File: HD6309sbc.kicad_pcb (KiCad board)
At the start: 4 copper layers, 99.8 x 99.8 mm, 63 parts, among them J1 Conn_01x02_Male, J2 Conn_02x30_Odd_Even, J3 Conn_01x02_Male, J4 Conn_01x07_Socket, J5 Conn_01x07_Socket, SW1 SW_Push, U1 HD63C09, U12 74HCT138, U16 74HCT541, U17 74HCT00, U18 74HCT04, U19 74HCT30, U2 DS1813, U3 74AHC1G14, U7 74HCT574

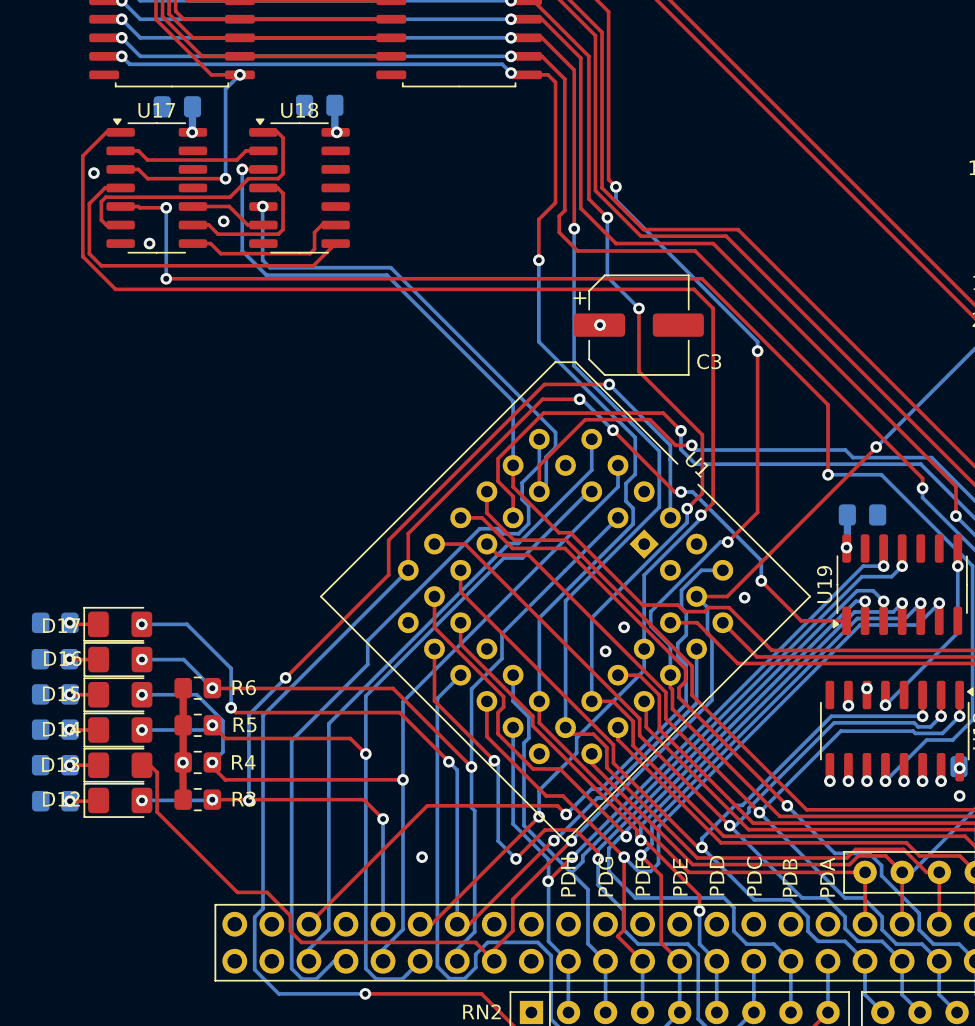
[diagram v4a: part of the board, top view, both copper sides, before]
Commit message: disambiguate register address
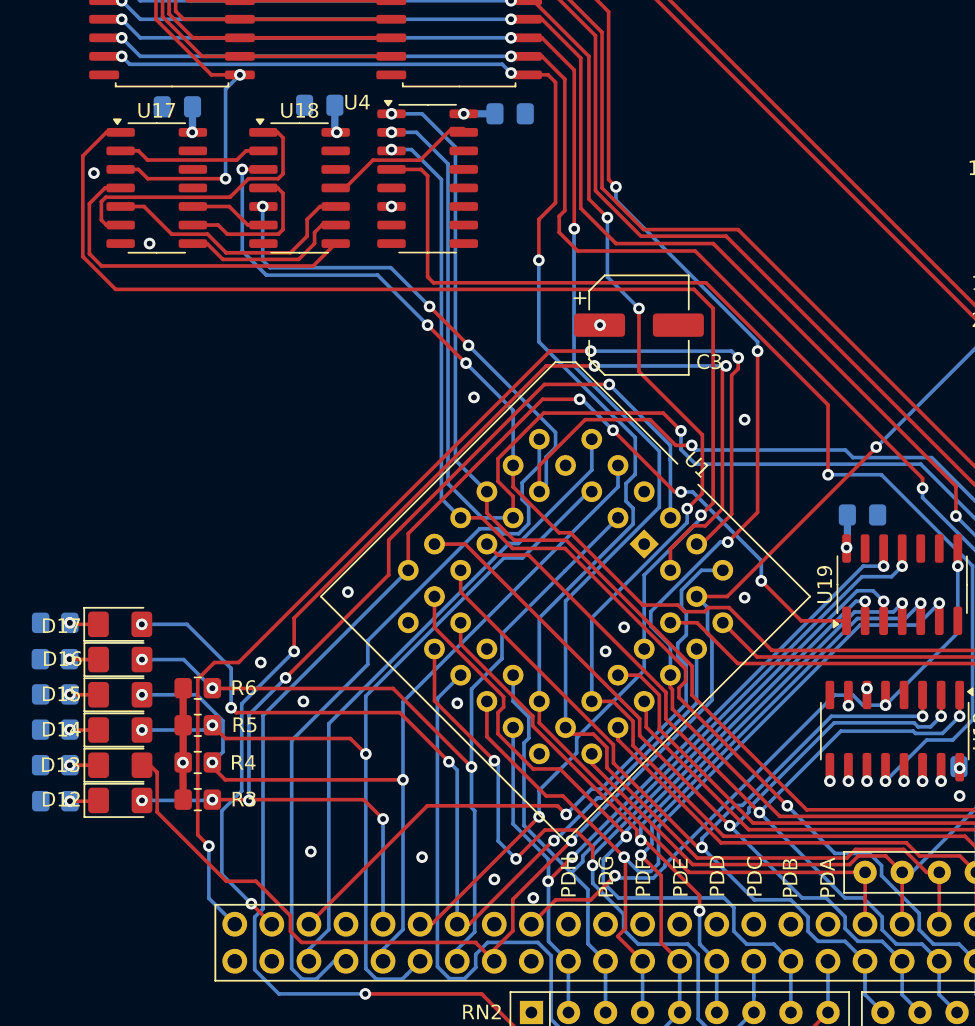
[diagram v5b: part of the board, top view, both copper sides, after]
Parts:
- added C8: 10uF, Capacitor_SMD:C_0805_2012Metric_Pad1.18x1.45mm_HandSolder, B.Cu at (64.1, 62.0)
- added U4: 74HCT138, Package_SO:SOIC-16_3.9x9.9mm_P1.27mm, F.Cu at (58.4, 66.4)
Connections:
- net /GPR1/~{SELPD0} renamed /GPR1/~{SELPD00}
- net SELPA renamed ~{SELPA}
- net SELPB renamed ~{SELPB}
- net SELPC renamed ~{SELPC}
- net SELPE renamed ~{SELPE}
- net SELPF renamed ~{SELPF}
- net SELPG renamed ~{SELPG}
- net SELPH renamed ~{SELPH}
- J2 pad 33: SELPD -> ~{SELPD}
- J2 pad 43: unconnected-(J2-Pin_43-Pad43) -> ~{MappedMem}
- J2 pad 57: unconnected-(J2-Pin_57-Pad57) -> TSC
- J2 pad 59: unconnected-(J2-Pin_59-Pad59) -> LIC
- U12 pad 12: SELPD -> ~{SELPD}
- U12 pad 5: /MemoryDecoder/MappedMem -> ~{MappedMem}
- U17 pad 5: SELPD -> Net-(U17-Pad5)
- U18 pad 10: unconnected-(U18-Pad10) -> Net-(U17-Pad5)
- U18 pad 11: unconnected-(U18-Pad11) -> ~{SELPD0}
- U19 pad 8: /MemoryDecoder/MappedMem -> ~{MappedMem}
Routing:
- net SELPD: track 109.3 -> 0.00 mm, vias 4 -> 0
- net ~{SELPD}: track 0.00 -> 92.8 mm, vias 0 -> 2
- net LIC: track 0.00 -> 78.5 mm, vias 0 -> 3
- net TSC: track 0.00 -> 77.2 mm, vias 0 -> 4
- net ~{MappedMem}: track 0.00 -> 44.7 mm, vias 0 -> 3
- net /A3: track 79.2 -> 111.3 mm, vias 1 -> 2
- net /A2: track 63.8 -> 93.6 mm, vias 1 -> 2
- net /A4: track 54.8 -> 82.8 mm, vias 1 -> 2
- net Net-(U17-Pad5): track 0.00 -> 18.0 mm
- net /MemoryDecoder/MappedMem: track 13.5 -> 0.00 mm, vias 2 -> 0
- net ~{SELPD0}: track 0.00 -> 10.5 mm
- net +5V: track 41.5 -> 43.7 mm, vias 10 -> 12
- net /A9: track 70.5 -> 71.3 mm
- net /A10: track 77.2 -> 77.8 mm
- net /A0: track 103.5 -> 103.1 mm, vias 2 -> 4
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
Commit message: tighten up tracing
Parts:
- moved C5 3.68 mm to (58.6, 47.8)
- moved U16 3.68 mm to (56.9, 53.6)
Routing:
- net /intD1: track 94.9 -> 113.3 mm
- net /intD0: track 100.2 -> 114.9 mm
- net /GPR1/W: track 73.3 -> 76.9 mm
- net /D0: track 132.1 -> 130.2 mm
- net /D2: track 146.5 -> 145.4 mm
- net /D1: track 154.4 -> 153.3 mm

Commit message: clean up before redesign
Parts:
- removed U17: 74HCT00, Package_SO:SOIC-14_3.9x8.7mm_P1.27mm
- removed U18: 74HCT04, Package_SO:SOIC-14_3.9x8.7mm_P1.27mm
- added C10: 10uF, Capacitor_SMD:C_0805_2012Metric_Pad1.18x1.45mm_HandSolder, B.Cu at (90.4, 47.9)
- added C9: 10uF, Capacitor_SMD:C_0805_2012Metric_Pad1.18x1.45mm_HandSolder, B.Cu at (78.3, 47.9)
- added D18: LED_Filled, LED_SMD:LED_1206_3216Metric_Pad1.42x1.75mm_HandSolder, F.Cu at (87.5, 37.6)
- added D19: LED_Filled, LED_SMD:LED_1206_3216Metric_Pad1.42x1.75mm_HandSolder, F.Cu at (85.1, 37.6)
- added D20: LED_Filled, LED_SMD:LED_1206_3216Metric_Pad1.42x1.75mm_HandSolder, F.Cu at (82.8, 37.6)
- added D21: LED_Filled, LED_SMD:LED_1206_3216Metric_Pad1.42x1.75mm_HandSolder, F.Cu at (80.4, 37.6)
- added D22: LED_Filled, LED_SMD:LED_1206_3216Metric_Pad1.42x1.75mm_HandSolder, F.Cu at (78.0, 37.6)
- added D23: LED_Filled, LED_SMD:LED_1206_3216Metric_Pad1.42x1.75mm_HandSolder, F.Cu at (75.6, 37.6)
- added D24: LED_Filled, LED_SMD:LED_1206_3216Metric_Pad1.42x1.75mm_HandSolder, F.Cu at (73.2, 37.6)
- added D25: LED_Filled, LED_SMD:LED_1206_3216Metric_Pad1.42x1.75mm_HandSolder, F.Cu at (70.8, 37.6)
- added J6: PD0, Connector_PinSocket_2.54mm:PinSocket_1x08_P2.54mm_Vertical, F.Cu at (62.0, 42.0)
- added J7: PD1, Connector_PinSocket_2.54mm:PinSocket_1x08_P2.54mm_Vertical, F.Cu at (88.0, 42.0)
- added R22: 470R, Resistor_SMD:R_0805_2012Metric_Pad1.20x1.40mm_HandSolder, B.Cu at (87.6, 33.5)
- added R23: 470R, Resistor_SMD:R_0805_2012Metric_Pad1.20x1.40mm_HandSolder, B.Cu at (85.1, 33.5)
- added R24: 470R, Resistor_SMD:R_0805_2012Metric_Pad1.20x1.40mm_HandSolder, B.Cu at (82.8, 33.5)
- added R25: 470R, Resistor_SMD:R_0805_2012Metric_Pad1.20x1.40mm_HandSolder, B.Cu at (80.4, 33.5)
- added R26: 470R, Resistor_SMD:R_0805_2012Metric_Pad1.20x1.40mm_HandSolder, B.Cu at (78.0, 33.5)
- added R27: 470R, Resistor_SMD:R_0805_2012Metric_Pad1.20x1.40mm_HandSolder, B.Cu at (75.6, 33.5)
- added R28: 470R, Resistor_SMD:R_0805_2012Metric_Pad1.20x1.40mm_HandSolder, B.Cu at (73.2, 33.5)
- added R29: 470R, Resistor_SMD:R_0805_2012Metric_Pad1.20x1.40mm_HandSolder, B.Cu at (70.8, 33.5)
- added U5: GAL16V8, Package_DIP:DIP-20_W7.62mm, F.Cu at (29.9, 71.3)
- added U6: 74HCT574, Package_SO:SOIC-20W_7.5x12.8mm_P1.27mm, F.Cu at (76.7, 53.6)
- added U8: 74HCT541, Package_SO:SOIC-20W_7.5x12.8mm_P1.27mm, F.Cu at (88.7, 53.6)
- moved C2 23.3 mm to (28.9, 68.6)
- moved C1 13.4 mm to (28.9, 66.4)
- moved C4 4.04 mm to (47.0, 47.9)
- moved U7 3.97 mm to (44.9, 53.6)
- moved R20 3.54 mm to (29.3, 99.3)
- moved D12 3.54 mm to (33.8, 109.0)
- moved D13 3.54 mm to (33.8, 106.6)
- moved D14 3.54 mm to (33.8, 104.2)
- moved D15 3.54 mm to (33.8, 101.8)
- moved D16 3.54 mm to (33.8, 99.4)
- moved D17 3.54 mm to (33.8, 97.0)
- moved R16 3.54 mm to (29.4, 109.1)
- moved R17 3.54 mm to (29.4, 106.6)
- moved R18 3.54 mm to (29.4, 104.2)
- moved R19 3.54 mm to (29.4, 101.8)
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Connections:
- net /intD0 renamed /ClockCard/intD00
- net /intD1 renamed /ClockCard/intD01
- net /intD2 renamed /ClockCard/intD02
- net /intD3 renamed /ClockCard/intD03
- net /intD4 renamed /ClockCard/intD04
- net /intD5 renamed /ClockCard/intD05
- net /intD6 renamed /ClockCard/intD06
- net /intD7 renamed /ClockCard/intD07
- U16 pad 1: /GPR1/W -> /GPR1/~{R}0
- U4 pad 10: unconnected-(U4-~{Y5}-Pad10) -> ~{SELPD5}
- U4 pad 11: unconnected-(U4-~{Y4}-Pad11) -> ~{SELPD4}
- U4 pad 12: unconnected-(U4-~{Y3}-Pad12) -> ~{SELPD3}
- U4 pad 13: unconnected-(U4-~{Y2}-Pad13) -> ~{SELPD2}
- U4 pad 14: unconnected-(U4-~{Y1}-Pad14) -> ~{SELPD1}
- U4 pad 7: unconnected-(U4-~{Y7}-Pad7) -> ~{SELPD7}
- U4 pad 9: unconnected-(U4-~{Y6}-Pad9) -> ~{SELPD6}
- U7 pad 11: /GPR1/W -> /GPR1/W0
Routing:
- net /GPR1/W: track 76.9 -> 0.00 mm, vias 2 -> 0
- net /GPR1/~{R}0: track 0.00 -> 71.0 mm
- net /GPR1/~{R}1: track 0.00 -> 65.5 mm, vias 0 -> 2
- net E: track 118.8 -> 176.8 mm, vias 2 -> 4
- net /GPR1/W1: track 0.00 -> 43.1 mm, vias 0 -> 2
- net /D0: track 130.2 -> 161.8 mm, vias 5 -> 7
- net /D3: track 123.7 -> 154.9 mm, vias 5 -> 7
- net /D4: track 140.0 -> 171.3 mm, vias 3 -> 5
- net /D2: track 145.4 -> 176.6 mm, vias 3 -> 5
- net /D1: track 153.3 -> 184.6 mm, vias 3 -> 5
- net /D5: track 118.3 -> 149.4 mm, vias 3 -> 5
- net /D6: track 137.4 -> 168.1 mm, vias 3 -> 5
- net /D7: track 112.3 -> 141.8 mm, vias 3 -> 5
- net /intD17: track 0.00 -> 28.6 mm
- net /intD16: track 0.00 -> 25.9 mm
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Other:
- board text added: "BUSY"
- board text added: "FIRQ"
- board text added: "GPR PD1"
- board text added: "HALT"
- board text added: "IRQ"
- board text added: "NMI"
- board text added: "RES"

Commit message: update readme
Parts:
- removed C1, C10, C2, C4, C5, C6, C7, C8, C9: 10uF, Capacitor_SMD:C_0805_2012Metric_Pad1.18x1.45mm_HandSolder
- removed D1: RED, LED_SMD:LED_0805_2012Metric_Pad1.15x1.40mm_HandSolder
- removed D10, D11, D12, D13, D14, D15, D16, D17, D18, D19, D20, D21, D22, D23, D24, D25, D4, D5, D6, D7, D8, D9: LED_Filled, LED_SMD:LED_1206_3216Metric_Pad1.42x1.75mm_HandSolder
- removed D2: YELLOW, LED_SMD:LED_0805_2012Metric_Pad1.15x1.40mm_HandSolder
- removed D3: GREEN, LED_SMD:LED_0805_2012Metric_Pad1.15x1.40mm_HandSolder
- removed J1, J3: Conn_01x02_Male, Connector_PinHeader_2.54mm:PinHeader_1x02_P2.54mm_Vertical
- removed R1, R10, R11, R12, R13, R14, R15, R16, R17, R18, R19, R20, R21, R22, R23, R24, R25, R26, R27, R28, R29: 470R, Resistor_SMD:R_0805_2012Metric_Pad1.20x1.40mm_HandSolder
- removed R2, R9: 330R, Resistor_SMD:R_0805_2012Metric_Pad1.20x1.40mm_HandSolder
- removed RN1, RN2, RN3: 4K7, Resistor_THT:R_Array_SIP9
- removed SW1: SW_Push, Button_Switch_SMD:SW_SPST_B3S-1000
- removed U12, U4: 74HCT138, Package_SO:SOIC-16_3.9x9.9mm_P1.27mm
- removed U16, U8: 74HCT541, Package_SO:SOIC-20W_7.5x12.8mm_P1.27mm
- removed U19: 74HCT30, Package_SO:SOIC-14_3.9x8.7mm_P1.27mm
- removed U2: DS1813, Package_TO_SOT_SMD:SOT-23-3
- removed U3: 74AHC1G14, Package_TO_SOT_SMD:SOT-353_SC-70-5_Handsoldering
- removed U5: GAL16V8, Package_DIP:DIP-20_W7.62mm
- removed U6, U7: 74HCT574, Package_SO:SOIC-20W_7.5x12.8mm_P1.27mm
- added J8: Interrupts, Connector_PinHeader_2.54mm:PinHeader_1x04_P2.54mm_Vertical, B.Cu at (79.6, 33.9)
- J2: value Conn_02x30_Odd_Even -> Address Bus; footprint Connector_PinHeader_2.54mm:PinHeader_2x30_P2.54mm_Vertical -> Connector_PinHeader_2.54mm:PinHeader_1x16_P2.54mm_Vertical; moved to B.Cu
- J4: value Conn_01x07_Socket -> Power; footprint Connector_PinSocket_2.54mm:PinSocket_1x07_P2.54mm_Vertical -> Connector_PinHeader_2.54mm:PinHeader_1x04_P2.54mm_Vertical; moved to B.Cu
- J5: value Conn_01x07_Socket -> quadrature; footprint Connector_PinSocket_2.54mm:PinSocket_1x07_P2.54mm_Vertical -> Connector_PinSocket_2.54mm:PinSocket_1x04_P2.54mm_Vertical; moved to B.Cu
- J6: value PD0 -> Data Bus; footprint Connector_PinSocket_2.54mm:PinSocket_1x08_P2.54mm_Vertical -> Connector_PinHeader_2.54mm:PinHeader_1x08_P2.54mm_Vertical; moved to B.Cu
- J7: value PD1 -> CPU Control; footprint Connector_PinSocket_2.54mm:PinSocket_1x08_P2.54mm_Vertical -> Connector_PinHeader_2.54mm:PinHeader_1x08_P2.54mm_Vertical; moved to B.Cu
- R7: value 470R -> 4.7k; moved to F.Cu
- R8: value 330R -> 4.7k
- moved J2 113.5 mm to (28.6, 48.6), turned to 180 degrees
- moved J4 81.8 mm to (28.6, 42.7), turned to 0 degrees
- moved J5 79.8 mm to (33.8, 86.9), turned to -90 degrees
- moved R5 74.1 mm to (73.9, 36.7)
- moved R4 74.1 mm to (73.9, 39.3)
- moved R3 71.8 mm to (73.9, 44.3)
- moved R6 67.2 mm to (73.9, 41.8)
- moved C3 41.9 mm to (48.2, 42.6), turned to 180 degrees
- moved R8 39.0 mm to (73.9, 46.9), turned to 0 degrees
- moved U1 36.4 mm to (58.2, 58.3)
- moved J6 32.9 mm to (79.4, 69.9), turned to 180 degrees
- moved J7 23.6 mm to (79.4, 63.9), turned to 0 degrees
- moved R7 14.9 mm to (73.9, 33.9), turned to 0 degrees
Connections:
- J2 pad 1: unconnected-(J2-Pin_1-Pad1) -> /A0
- J2 pad 10: Q -> /A9
- J2 pad 11: /D0 -> /A10
- J2 pad 12: /A0 -> /A11
- J2 pad 13: /D1 -> /A12
- J2 pad 14: /A1 -> /A13
- J2 pad 15: /D2 -> /A14
- J2 pad 16: /A2 -> /A15
- J2 pad 2: +5V -> /A1
- J2 pad 3: Clock24 -> /A2
- J2 pad 4: Clock3 -> /A3
- J2 pad 5: Clock12 -> /A4
- J2 pad 6: Clock6 -> /A5
- J2 pad 7: ~{E} -> /A6
- J2 pad 8: E -> /A7
- J2 pad 9: ~{Q} -> /A8
- J4 pad 1: /ClockCard/intD00 -> GND
- J4 pad 2: /ClockCard/intD01 -> +5V
- J4 pad 3: Clock24 -> +5V
- J4 pad 4: Clock12 -> GND
- J5 pad 1: GND -> E
- J5 pad 2: E -> unconnected-(J5-Pin_2-Pad2)
- J5 pad 3: ~{E} -> ~{RESET}
- J5 pad 4: ~{RESET} -> Q
- J6 pad 1: /ClockCard/intD00 -> /D0
- J6 pad 2: /ClockCard/intD01 -> /D1
- J6 pad 3: /ClockCard/intD02 -> /D2
- J6 pad 4: /ClockCard/intD03 -> /D3
- J6 pad 5: /ClockCard/intD04 -> /D4
- J6 pad 6: /ClockCard/intD05 -> /D5
- J6 pad 7: /ClockCard/intD06 -> /D6
- J6 pad 8: /ClockCard/intD07 -> /D7
- J7 pad 1: /intD10 -> BUSY
- J7 pad 2: /intD11 -> R/~{W}
- J7 pad 3: /intD12 -> ~{HALT}
- J7 pad 4: /intD13 -> AVMA
- J7 pad 5: /intD14 -> TSC
- J7 pad 6: /intD15 -> LIC
- J7 pad 7: /intD16 -> BS
- J7 pad 8: /intD17 -> BA
- R7 pad 1: Net-(D5-K) -> +5V
- R7 pad 2: GND -> ~{RESET}
- R8 pad 1: Net-(D2-K) -> TSC
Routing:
- net /D1: track 184.6 -> 25.2 mm, vias 5 -> 0
- net /D2: track 176.6 -> 23.7 mm, vias 5 -> 0
- net /D4: track 171.3 -> 26.8 mm, vias 5 -> 0
- net /D0: track 161.8 -> 20.5 mm, vias 7 -> 0
- net E: track 176.8 -> 36.4 mm, vias 4 -> 0
- net /D6: track 168.1 -> 30.0 mm, vias 5 -> 0
- net /D3: track 154.9 -> 28.3 mm, vias 7 -> 0
- net /D5: track 149.4 -> 31.5 mm, vias 5 -> 0
- net /ClockCard/intD00: track 111.2 -> 0.00 mm, vias 2 -> 0
- net /ClockCard/intD01: track 107.9 -> 0.00 mm, vias 2 -> 0
- net /D7: track 141.8 -> 37.4 mm, vias 5 -> 0
- net /A8: track 120.9 -> 17.1 mm, vias 5 -> 0
- net /A1: track 118.5 -> 23.9 mm, vias 3 -> 0
- net ~{SELPD}: track 91.7 -> 0.00 mm, vias 2 -> 0
- net /A3: track 112.8 -> 21.7 mm, vias 2 -> 0
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- removed copper zone on In2.Cu, net +5V
- removed copper zone on In1.Cu, net GND
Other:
- board size 99.8 x 99.8 mm -> 55.2 x 58.7 mm
- copper layers 4 -> 2
- board text added: "6309 SBC Rev 3.1"
- board text added: "A0"
- board text added: "A1"
- board text added: "A10"
- board text added: "A11"
- board text added: "A12"
- board text added: "A13"
- board text added: "A14"
- board text added: "A15"
- board text added: "A2"
- board text added: "A3"
- board text added: "A4"
- board text added: "A5"
- board text added: "A6"
- board text added: "A7"
- board text added: "A8"
- board text added: "A9"
- board text added: "AVMA"
- board text added: "BA"
- board text added: "BS"
- board text added: "D0"
- board text added: "D1"
- board text added: "D2"
- board text added: "D3"
- board text added: "D4"
- board text added: "D5"
- board text added: "D6"
- board text added: "D7"
- board text added: "LIC"
- board text added: "R/~{W}"
- board text added: "TSC"
- board text added: "~{HALT}"
- board text removed: "1.5x"
- board text removed: "12x"
- board text removed: "24x"
- board text removed: "3x"
- board text removed: "6309 SBC Rev 2.0"
- board text removed: "6x"
- board text removed: "Clock Card"
- board text removed: "GPR PD0"
- board text removed: "GPR PD1"
- board text removed: "PDA"
- board text removed: "PDB"
- board text removed: "PDC"
- board text removed: "PDD"
- board text removed: "PDE"
- board text removed: "PDF"
- board text removed: "PDG"
- board text removed: "PDH"
- board text removed: "~{E}"
- board text removed: "~{Q}"
- board text removed: "~{RESET}"
